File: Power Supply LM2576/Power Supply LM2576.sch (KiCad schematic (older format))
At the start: 14 parts, among them J1 Power IN, J2 Power OUT, Q1 IRLML0030, U1 LM2576T-ADJ

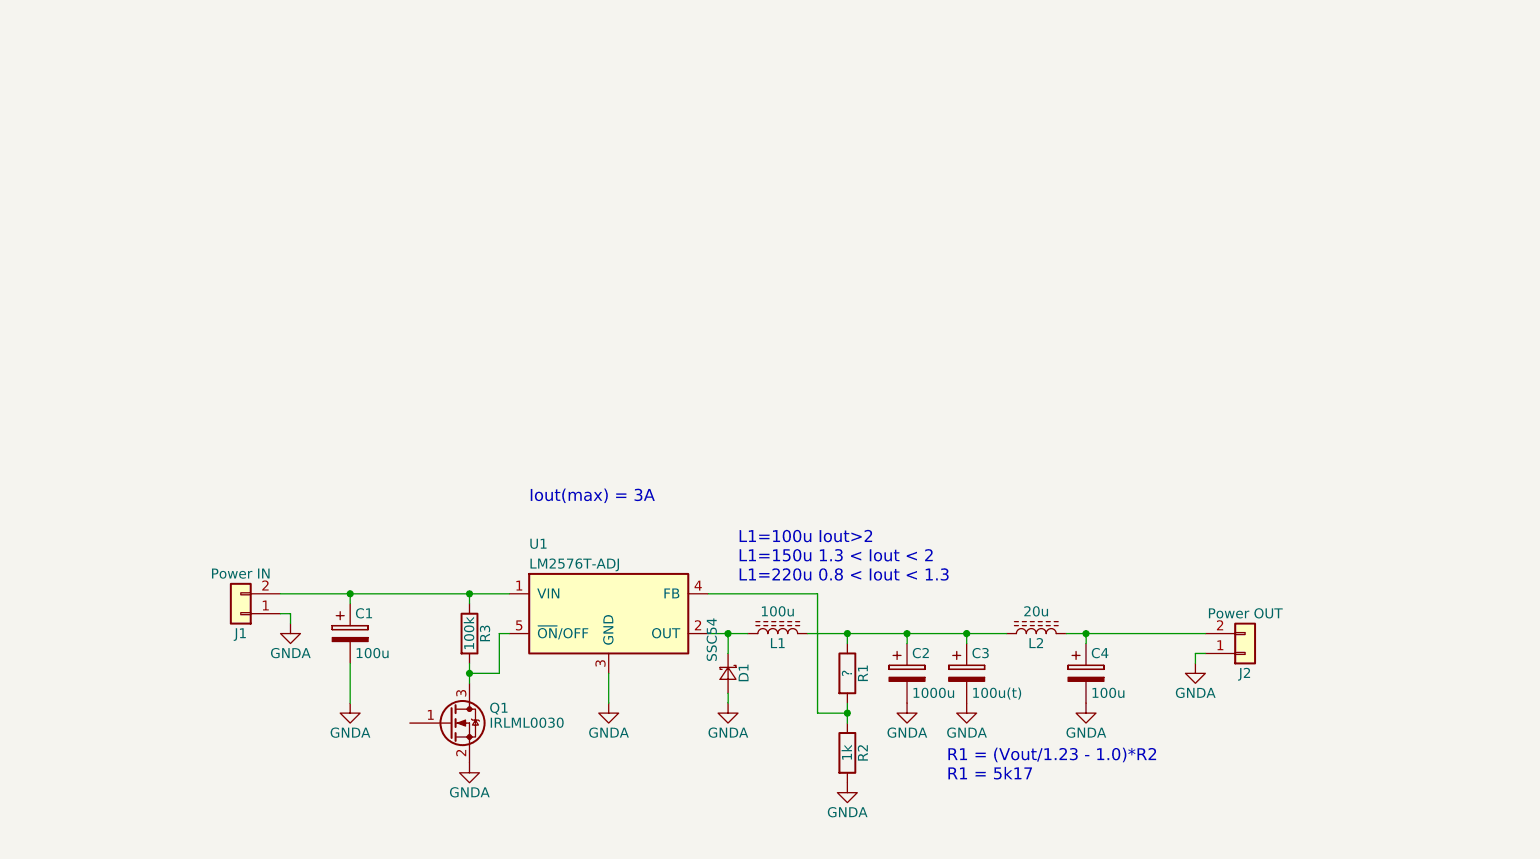
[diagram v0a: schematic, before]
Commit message: ADC added for monitoring
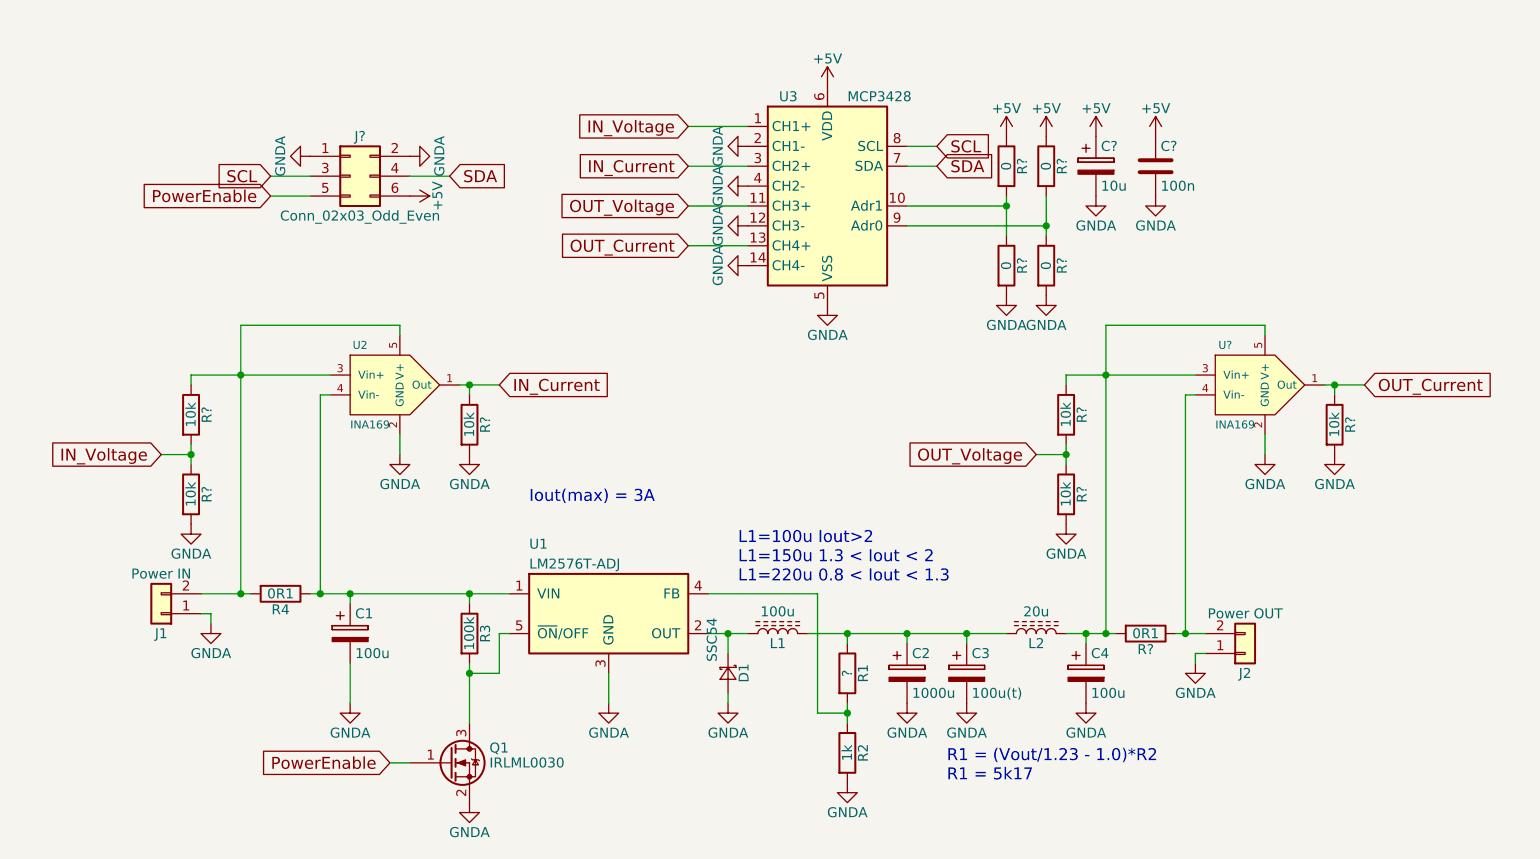
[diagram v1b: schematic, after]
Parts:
- added C?: 10u, Capacitors_THT:CP_Radial_D8.0mm_P2.50mm, symbol CP
- added C?: 100n, symbol C
- added J?: Conn_02x03_Odd_Even, symbol Conn_02x03_Odd_Even
- added R4, R?: 0R1, Resistors_SMD:R_2512, symbol R
- added R? (x6): 10k, Resistors_SMD:R_0805, symbol R
- added R? (x4): 0, Resistors_SMD:R_0805, symbol R
- added U2, U?: INA169, symbol INA169
- added U3: MCP3428, symbol MCP3428
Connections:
- net GNDA: now also C?.2, C?.2, J?.1 (Pin_1), J?.2 (Pin_2), R?.2, R?.2, R?.2, R?.2, R?.2, R?.2, U2.2 (GND), U3.12 (CH3-), U3.14 (CH4-), U3.2 (CH1-), U3.4 (CH2-), U3.5 (VSS), U?.2 (GND)
- net at C1.1, R3.1, U1.1 (VIN): now also R4.1, U2.4 (Vin-); no longer J1.2 (Pin_2)
- net at C4.1, L2.2: now also R?.1, R?.2, U?.3 (Vin+), U?.5 (V+); no longer J2.2 (Pin_2)
- net PowerEnable: now reaches Q1.1 (G)
- net PowerEnable: now also J?.5 (Pin_5)
- new net: J1.2 (Pin_2), R4.2, R?.1, U2.3 (Vin+), U2.5 (V+)
- new net: J2.2 (Pin_2), R?.1, U?.4 (Vin-)
- new net: R?.1, R?.2, U3.10 (Adr1)
- new net: R?.1, R?.2, U3.9 (Adr0)
- new net +5V: C?.1, C?.1, J?.6 (Pin_6), R?.1, R?.1, U3.6 (VDD)
- new net IN_Current: R?.1, U2.1 (Out), U3.3 (CH2+)
- new net IN_Voltage: R?.1, R?.2, U3.1 (CH1+)
- new net OUT_Current: R?.1, U3.13 (CH4+), U?.1 (Out)
- new net OUT_Voltage: R?.1, R?.2, U3.11 (CH3+)
- new net SCL: J?.3 (Pin_3), U3.8 (SCL)
- new net SDA: J?.4 (Pin_4), U3.7 (SDA)
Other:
- moved on the sheet: J1, Q1

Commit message: PCB init
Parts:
- C2: footprint Capacitors_THT:CP_Radial_D12.5mm_P5.00mm -> Capacitors_THT:CP_Radial_D10.0mm_P2.50mm
- C3: footprint Capacitors_THT:CP_Radial_D12.5mm_P5.00mm -> Capacitors_Tantalum_SMD:CP_Tantalum_Case-D_EIA-7343-31_Reflow
- C4: footprint Capacitors_THT:CP_Radial_D12.5mm_P5.00mm -> Capacitors_THT:CP_Radial_D6.3mm_P2.50mm
- C5: renamed from C?; footprint Capacitors_THT:CP_Radial_D8.0mm_P2.50mm -> Capacitors_THT:CP_Radial_D6.3mm_P2.50mm
- C6: renamed from C?; footprint (none) -> Capacitors_SMD:C_0805
- J2: renamed from J?; footprint (none) -> Socket_Strips:Socket_Strip_Straight_2x03_Pitch2.54mm
- L1: footprint Inductors_THT:L_Toroid_Vertical_L21.6mm_W8.4mm_P8.38mm_Pulse_G -> Inductors_THT:L_Toroid_Vertical_L26.7mm_W14.0mm_P10.16mm_Pulse_D
- L2: footprint Inductors_THT:L_Toroid_Vertical_L10.0mm_W5.0mm_P5.08mm -> Inductors_THT:L_Toroid_Vertical_L16.8mm_W9.2mm_P7.10mm_Vishay_TJ3
- U1: renamed from U2; footprint (none) -> TO_SOT_Packages_SMD:SOT-23-5
- U2: renamed from U1; footprint TO_SOT_Packages_THT:TO-220-5_Pentawatt_Multiwatt-5_Vertical -> TO_SOT_Packages_THT:TO-220-5_Vertical_StaggeredType1
- U3: footprint (none) -> Housings_SOIC:SOIC-14_3.9x8.7mm_Pitch1.27mm
- U4: renamed from U?; footprint (none) -> TO_SOT_Packages_SMD:SOT-23-5
- gave numbers to parts that had none: 11
- renumbered J2 to J3, R4 to R3, R3 to R5, R1 to R6, R2 to R7
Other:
- note added: "Uref=2024mV"

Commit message: Some work on PCB
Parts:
- added R16, R17, R18, R19: 0R1, Resistors_SMD:R_2512, symbol R
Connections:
- net IN_Current: now also U3.13 (CH4+); no longer U3.3 (CH2+)
- net IN_Voltage: now also U3.11 (CH3+); no longer U3.1 (CH1+)
- net OUT_Current: now also U3.3 (CH2+); no longer U3.13 (CH4+)
- net OUT_Voltage: now also U3.1 (CH1+); no longer U3.11 (CH3+)
- net at C1.1, R3.1, R5.1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: now also R16.1, R17.1
- net at J1.2 (Pin_2), R1.1, R3.2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: now also R16.2, R17.2
- net at J3.2 (Pin_2), R14.1, U4.4 (Vin-): now also R18.1, R19.1
- net at C4.1, L2.2, R12.1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: now also R18.2, R19.2
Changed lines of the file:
@@
 $EndComp
 $Comp
-L GNDA #PWR01
+L GNDA #PWR10
 U 1 1 59FFC0A0
 P 5050 4200
-F 0 "#PWR01" H 5050 3950 50  0001 C CNN
+F 0 "#PWR10" H 5050 3950 50  0001 C CNN
 F 1 "GNDA" H 5050 4050 50  0000 C CNN
 F 2 "" H 5050 4200 50  0001 C CNN
@@
 $EndComp
 $Comp
-L GNDA #PWR02
+L GNDA #PWR19
 U 1 1 59FFC329
 P 6550 4200
-F 0 "#PWR02" H 6550 3950 50  0001 C CNN
+F 0 "#PWR19" H 6550 3950 50  0001 C CNN
 F 1 "GNDA" H 6550 4050 50  0000 C CNN
 F 2 "" H 6550 4200 50  0001 C CNN
@@
 $EndComp
 $Comp
-L GNDA #PWR03
+L GNDA #PWR18
 U 1 1 59FFC346
 P 6250 4600
-F 0 "#PWR03" H 6250 4350 50  0001 C CNN
+F 0 "#PWR18" H 6250 4350 50  0001 C CNN
 F 1 "GNDA" H 6250 4450 50  0000 C CNN
 F 2 "" H 6250 4600 50  0001 C CNN
@@
 $EndComp
 $Comp
-L GNDA #PWR04
+L GNDA #PWR4
 U 1 1 59FFC406
 P 3750 4200
-F 0 "#PWR04" H 3750 3950 50  0001 C CNN
+F 0 "#PWR4" H 3750 3950 50  0001 C CNN
 F 1 "GNDA" H 3750 4050 50  0000 C CNN
 F 2 "" H 3750 4200 50  0001 C CNN
@@
 $EndComp
 $Comp
-L GNDA #PWR05
+L GNDA #PWR2
 U 1 1 59FFC542
 P 3050 3800
-F 0 "#PWR05" H 3050 3550 50  0001 C CNN
+F 0 "#PWR2" H 3050 3550 50  0001 C CNN
 F 1 "GNDA" H 3050 3650 50  0000 C CNN
 F 2 "" H 3050 3800 50  0001 C CNN
@@
 $EndComp
 $Comp
-L GNDA #PWR06
+L GNDA #PWR31
 U 1 1 59FFC652
 P 8000 4000
-F 0 "#PWR06" H 8000 3750 50  0001 C CNN
+F 0 "#PWR31" H 8000 3750 50  0001 C CNN
 F 1 "GNDA" H 8000 3850 50  0000 C CNN
 F 2 "" H 8000 4000 50  0001 C CNN
@@
 $EndComp
 $Comp
-L GNDA #PWR07
+L GNDA #PWR11
 U 1 1 59FFC8D5
 P 5650 4200
-F 0 "#PWR07" H 5650 3950 50  0001 C CNN
+F 0 "#PWR11" H 5650 3950 50  0001 C CNN
 F 1 "GNDA" H 5650 4050 50  0000 C CNN
 F 2 "" H 5650 4200 50  0001 C CNN
@@
 $EndComp
 $Comp
-L GNDA #PWR08
+L GNDA #PWR9
 U 1 1 5A0254E4
 P 4350 4700
-F 0 "#PWR08" H 4350 4450 50  0001 C CNN
+F 0 "#PWR9" H 4350 4450 50  0001 C CNN
 F 1 "GNDA" H 4350 4550 50  0000 C CNN
 F 2 "" H 4350 4700 50  0001 C CNN
@@
 $EndComp
 $Comp
-L GNDA #PWR09
+L GNDA #PWR20
 U 1 1 5A025A22
 P 6850 4200
-F 0 "#PWR09" H 6850 3950 50  0001 C CNN
+F 0 "#PWR20" H 6850 3950 50  0001 C CNN
 F 1 "GNDA" H 6850 4050 50  0000 C CNN
 F 2 "" H 6850 4200 50  0001 C CNN
@@
 $EndComp
 $Comp
-L GNDA #PWR010
+L GNDA #PWR26
 U 1 1 5A025EC7
 P 7450 4200
-F 0 "#PWR010" H 7450 3950 50  0001 C CNN
+F 0 "#PWR26" H 7450 3950 50  0001 C CNN
 F 1 "GNDA" H 7450 4050 50  0000 C CNN
 F 2 "" H 7450 4200 50  0001 C CNN
@@
 Connection ~ 3600 3650
 $Comp
-L GNDA #PWR011
+L GNDA #PWR5
 U 1 1 5A03B368
 P 4000 2950
-F 0 "#PWR011" H 4000 2700 50  0001 C CNN
+F 0 "#PWR5" H 4000 2700 50  0001 C CNN
 F 1 "GNDA" H 4000 2800 50  0000 C CNN
 F 2 "" H 4000 2950 50  0001 C CNN
@@
 	4350 2600 4350 2650
 $Comp
-L GNDA #PWR012
+L GNDA #PWR8
 U 1 1 5A03B53A
 P 4350 2950
-F 0 "#PWR012" H 4350 2700 50  0001 C CNN
+F 0 "#PWR8" H 4350 2700 50  0001 C CNN
 F 1 "GNDA" H 4350 2800 50  0000 C CNN
 F 2 "" H 4350 2950 50  0001 C CNN
@@
 	7950 2650 8000 2650
 $Comp
-L GNDA #PWR013
+L GNDA #PWR32
 U 1 1 5A03B8EA
 P 8350 2950
-F 0 "#PWR013" H 8350 2700 50  0001 C CNN
+F 0 "#PWR32" H 8350 2700 50  0001 C CNN
 F 1 "GNDA" H 8350 2800 50  0000 C CNN
 F 2 "" H 8350 2950 50  0001 C CNN
@@
 	8700 2600 8700 2650
 $Comp
-L GNDA #PWR014
+L GNDA #PWR33
 U 1 1 5A03B8F8
 P 8700 2950
-F 0 "#PWR014" H 8700 2700 50  0001 C CNN
+F 0 "#PWR33" H 8700 2700 50  0001 C CNN
 F 1 "GNDA" H 8700 2800 50  0000 C CNN
 F 2 "" H 8700 2950 50  0001 C CNN
@@
 $EndComp
 $Comp
-L +5V #PWR015
+L +5V #PWR27
 U 1 1 5A03C42C
 P 7500 1350
-F 0 "#PWR015" H 7500 1200 50  0001 C CNN
+F 0 "#PWR27" H 7500 1200 50  0001 C CNN
 F 1 "+5V" H 7500 1490 50  0000 C CNN
 F 2 "" H 7500 1350 50  0001 C CNN
@@
 $EndComp
 $Comp
-L +5V #PWR016
+L +5V #PWR29
 U 1 1 5A03C4F6
 P 7800 1350
-F 0 "#PWR016" H 7800 1200 50  0001 C CNN
+F 0 "#PWR29" H 7800 1200 50  0001 C CNN
 F 1 "+5V" H 7800 1490 50  0000 C CNN
 F 2 "" H 7800 1350 50  0001 C CNN
@@
 $EndComp
 $Comp
-L +5V #PWR017
+L +5V #PWR16
 U 1 1 5A03C65A
 P 6150 1100
-F 0 "#PWR017" H 6150 950 50  0001 C CNN
+F 0 "#PWR16" H 6150 950 50  0001 C CNN
 F 1 "+5V" H 6150 1240 50  0000 C CNN
 F 2 "" H 6150 1100 50  0001 C CNN
@@
 $EndComp
 $Comp
-L GNDA #PWR018
+L GNDA #PWR30
 U 1 1 5A03CBEF
 P 7800 1650
-F 0 "#PWR018" H 7800 1400 50  0001 C CNN
+F 0 "#PWR30" H 7800 1400 50  0001 C CNN
 F 1 "GNDA" H 7800 1500 50  0000 C CNN
 F 2 "" H 7800 1650 50  0001 C CNN
@@
 $EndComp
 $Comp
-L GNDA #PWR019
+L GNDA #PWR28
 U 1 1 5A03CC3F
 P 7500 1650
-F 0 "#PWR019" H 7500 1400 50  0001 C CNN
+F 0 "#PWR28" H 7500 1400 50  0001 C CNN
 F 1 "GNDA" H 7500 1500 50  0000 C CNN
 F 2 "" H 7500 1650 50  0001 C CNN
@@
 $EndComp
 $Comp
-L GNDA #PWR020
+L GNDA #PWR17
 U 1 1 5A03CC8F
 P 6150 2200
-F 0 "#PWR020" H 6150 1950 50  0001 C CNN
+F 0 "#PWR17" H 6150 1950 50  0001 C CNN
 F 1 "GNDA" H 6150 2050 50  0000 C CNN
 F 2 "" H 6150 2200 50  0001 C CNN
@@
 $EndComp
 $Comp
-L GNDA #PWR021
+L GNDA #PWR12
 U 1 1 5A03CD97
 P 5750 1400
-F 0 "#PWR021" H 5750 1150 50  0001 C CNN
+F 0 "#PWR12" H 5750 1150 50  0001 C CNN
 F 1 "GNDA" H 5750 1250 50  0000 C CNN
 F 2 "" H 5750 1400 50  0001 C CNN
@@
 $EndComp
 $Comp
-L GNDA #PWR022
+L GNDA #PWR13
 U 1 1 5A03CE34
 P 5750 1600
-F 0 "#PWR022" H 5750 1350 50  0001 C CNN
+F 0 "#PWR13" H 5750 1350 50  0001 C CNN
 F 1 "GNDA" H 5750 1450 50  0000 C CNN
 F 2 "" H 5750 1600 50  0001 C CNN
@@
 $EndComp
 $Comp
-L GNDA #PWR023
+L GNDA #PWR14
 U 1 1 5A03CE84
 P 5750 1800
-F 0 "#PWR023" H 5750 1550 50  0001 C CNN
+F 0 "#PWR14" H 5750 1550 50  0001 C CNN
 F 1 "GNDA" H 5750 1650 50  0000 C CNN
 F 2 "" H 5750 1800 50  0001 C CNN
@@
 $EndComp
 $Comp
-L GNDA #PWR024
+L GNDA #PWR15
 U 1 1 5A03CED4
 P 5750 2000
-F 0 "#PWR024" H 5750 1750 50  0001 C CNN
+F 0 "#PWR15" H 5750 1750 50  0001 C CNN
 F 1 "GNDA" H 5750 1850 50  0000 C CNN
 F 2 "" H 5750 2000 50  0001 C CNN
@@
 OUT_Current
 Connection ~ 8700 2600
+Text GLabel 5450 1900 0    60   Input ~ 0
+IN_Current
 Text GLabel 5450 1500 0    60   Input ~ 0
-IN_Current
-Text GLabel 5450 1900 0    60   Input ~ 0
 OUT_Current
 Wire Wire Line
@@
 $EndComp
 $Comp
-L GNDA #PWR025
+L GNDA #PWR1
 U 1 1 5A03E32E
 P 2950 3300
-F 0 "#PWR025" H 2950 3050 50  0001 C CNN
+F 0 "#PWR1" H 2950 3050 50  0001 C CNN
 F 1 "GNDA" H 2950 3150 50  0000 C CNN
 F 2 "" H 2950 3300 50  0001 C CNN
@@
 $EndComp
 $Comp
-L GNDA #PWR026
+L GNDA #PWR25
 U 1 1 5A03E84E
 P 7350 3300
-F 0 "#PWR026" H 7350 3050 50  0001 C CNN
+F 0 "#PWR25" H 7350 3050 50  0001 C CNN
 F 1 "GNDA" H 7350 3150 50  0000 C CNN
 F 2 "" H 7350 3300 50  0001 C CNN
@@
 Wire Wire Line
 	7350 2600 7350 2550
+Text GLabel 5450 1300 0    60   Input ~ 0
+OUT_Voltage
 Text GLabel 5450 1700 0    60   Input ~ 0
-OUT_Voltage
-Text GLabel 5450 1300 0    60   Input ~ 0
 IN_Voltage
 Wire Wire Line
@@
 Connection ~ 7050 1700
 $Comp
-L GNDA #PWR027
+L GNDA #PWR22
 U 1 1 5A03F4A2
 P 7050 2150
-F 0 "#PWR027" H 7050 1900 50  0001 C CNN
+F 0 "#PWR22" H 7050 1900 50  0001 C CNN
 F 1 "GNDA" H 7050 2000 50  0000 C CNN
 F 2 "" H 7050 2150 50  0001 C CNN
@@
 $EndComp
 $Comp
-L +5V #PWR028
+L +5V #PWR21
 U 1 1 5A03F504
 P 7050 1350
-F 0 "#PWR028" H 7050 1200 50  0001 C CNN
+F 0 "#PWR21" H 7050 1200 50  0001 C CNN
 F 1 "+5V" H 7050 1490 50  0000 C CNN
 F 2 "" H 7050 1350 50  0001 C CNN
@@
 Connection ~ 7250 1800
 $Comp
-L GNDA #PWR029
+L GNDA #PWR24
 U 1 1 5A03F5DF
 P 7250 2150
-F 0 "#PWR029" H 7250 1900 50  0001 C CNN
+F 0 "#PWR24" H 7250 1900 50  0001 C CNN
 F 1 "GNDA" H 7250 2000 50  0000 C CNN
 F 2 "" H 7250 2150 50  0001 C CNN
@@
 $EndComp
 $Comp
-L +5V #PWR030
+L +5V #PWR23
 U 1 1 5A03F5E5
 P 7250 1350
-F 0 "#PWR030" H 7250 1200 50  0001 C CNN
+F 0 "#PWR23" H 7250 1200 50  0001 C CNN
 F 1 "+5V" H 7250 1490 50  0000 C CNN
 F 2 "" H 7250 1350 50  0001 C CNN
@@
 $EndComp
 $Comp
-L GNDA #PWR031
+L GNDA #PWR3
 U 1 1 5A03FA4A
 P 3550 1450
-F 0 "#PWR031" H 3550 1200 50  0001 C CNN
+F 0 "#PWR3" H 3550 1200 50  0001 C CNN
 F 1 "GNDA" H 3550 1300 50  0000 C CNN
 F 2 "" H 3550 1450 50  0001 C CNN
@@
 $EndComp
 $Comp
-L +5V #PWR032
+L +5V #PWR7
 U 1 1 5A03FAB5
 P 4050 1650
-F 0 "#PWR032" H 4050 1500 50  0001 C CNN
+F 0 "#PWR7" H 4050 1500 50  0001 C CNN
 F 1 "+5V" H 4050 1790 50  0000 C CNN
 F 2 "" H 4050 1650 50  0001 C CNN
@@
 $EndComp
 $Comp
-L GNDA #PWR033
+L GNDA #PWR6
 U 1 1 5A03FDB0
 P 4050 1450
-F 0 "#PWR033" H 4050 1200 50  0001 C CNN
+F 0 "#PWR6" H 4050 1200 50  0001 C CNN
 F 1 "GNDA" H 4050 1300 50  0000 C CNN
 F 2 "" H 4050 1450 50  0001 C CNN
@@
 Text Notes 5850 850  0    60   ~ 0
 Uref=2024mV
+$Comp
+L R R17
+U 1 1 5A20C4E2
+P 3400 3550
+F 0 "R17" V 3480 3550 50  0000 C CNN
+F 1 "0R1" V 3400 3550 50  0000 C CNN
+F 2 "Resistors_SMD:R_2512" V 3330 3550 50  0001 C CNN
+F 3 "" H 3400 3550 50  0001 C CNN
+	1    3400 3550
+	0    1    1    0
+$EndComp
+$Comp
+L R R16
+U 1 1 5A20C55D
+P 3400 3450
+F 0 "R16" V 3480 3450 50  0000 C CNN
+F 1 "0R1" V 3400 3450 50  0000 C CNN
+F 2 "Resistors_SMD:R_2512" V 3330 3450 50  0001 C CNN
+F 3 "" H 3400 3450 50  0001 C CNN
+	1    3400 3450
+	0    1    1    0
+$EndComp
+Wire Wire Line
+	3250 3450 3200 3450
+Connection ~ 3200 3450
+Wire Wire Line
+	3250 3550 3200 3550
+Connection ~ 3200 3550
+Wire Wire Line
+	3550 3550 3600 3550
+Connection ~ 3600 3550
+Wire Wire Line
+	3550 3450 3600 3450
+Connection ~ 3600 3450
+$Comp
+L R R19
+U 1 1 5A20C8E3
+P 7750 3750
+F 0 "R19" V 7830 3750 50  0000 C CNN
+F 1 "0R1" V 7750 3750 50  0000 C CNN
+F 2 "Resistors_SMD:R_2512" V 7680 3750 50  0001 C CNN
+F 3 "" H 7750 3750 50  0001 C CNN
+	1    7750 3750
+	0    1    1    0
+$EndComp
+$Comp
+L R R18
+U 1 1 5A20C960
+P 7750 3650
+F 0 "R18" V 7830 3650 50  0000 C CNN
+F 1 "0R1" V 7750 3650 50  0000 C CNN
+F 2 "Resistors_SMD:R_2512" V 7680 3650 50  0001 C CNN
+F 3 "" H 7750 3650 50  0001 C CNN
+	1    7750 3650
+	0    1    1    0
+$EndComp
+Wire Wire Line
+	7600 3650 7550 3650
+Connection ~ 7550 3650
+Wire Wire Line
+	7550 3750 7600 3750
+Connection ~ 7550 3750
+Wire Wire Line
+	7900 3750 7950 3750
+Connection ~ 7950 3750
+Wire Wire Line
+	7900 3650 7950 3650
+Connection ~ 7950 3650
 $EndSCHEMATC
